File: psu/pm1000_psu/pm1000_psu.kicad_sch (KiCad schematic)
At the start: 42 parts, among them J1 , J2 , J3 , J4 , J5 , U1 LM317_TO-220, U2 LM317_TO-220, U3 LM317_TO-220

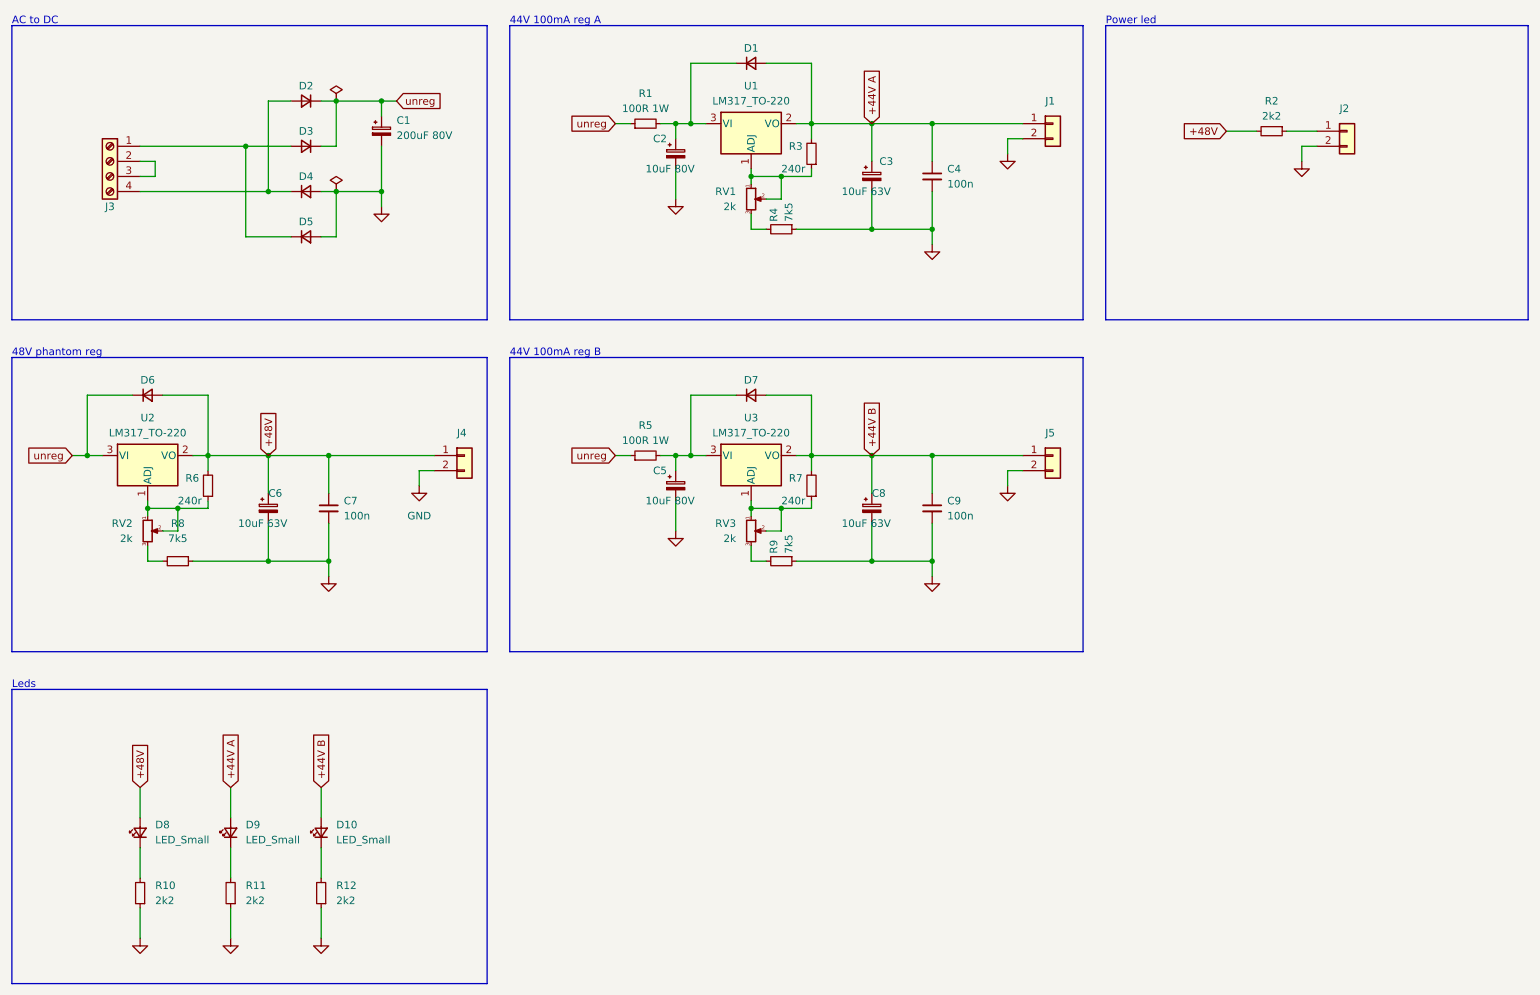
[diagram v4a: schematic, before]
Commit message: route psu pcb
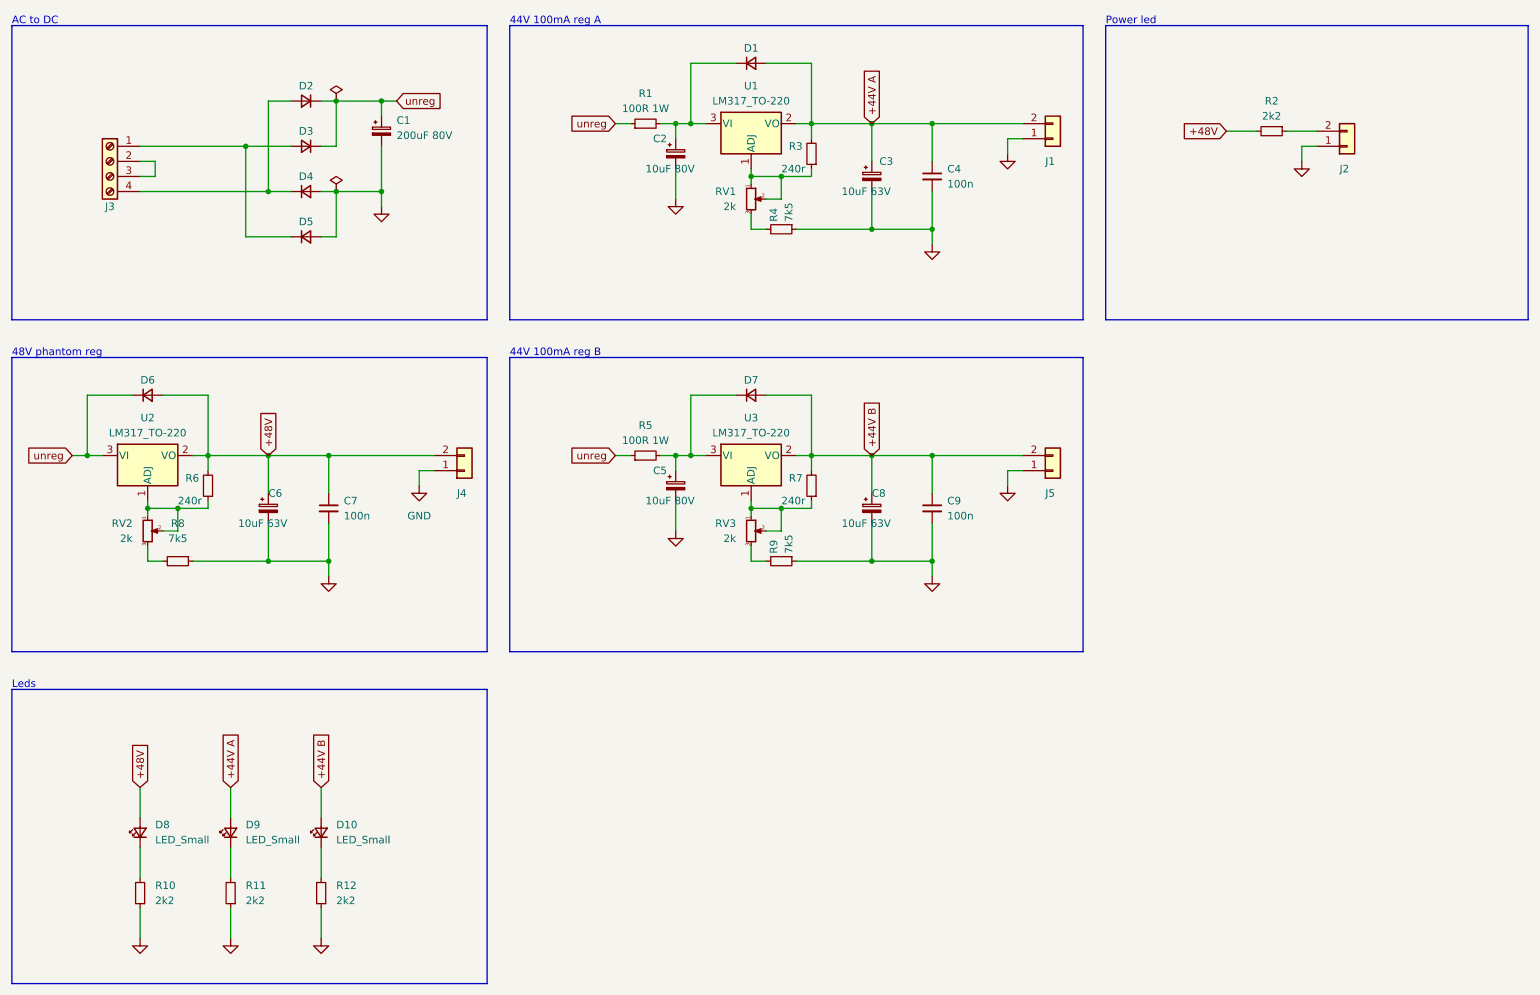
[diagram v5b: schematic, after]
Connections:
- net +44V A: now also J1.2 (Pin_2); no longer J1.1 (Pin_1)
- net +44V B: now also J5.2 (Pin_2); no longer J5.1 (Pin_1)
- net +48V: now also J4.2 (Pin_2); no longer J4.1 (Pin_1)
- net GND: now also J1.1 (Pin_1), J2.1 (Pin_1), J4.1 (Pin_1), J5.1 (Pin_1); no longer J1.2 (Pin_2), J2.2 (Pin_2), J4.2 (Pin_2), J5.2 (Pin_2)
- net at R2.1: now also J2.2 (Pin_2); no longer J2.1 (Pin_1)
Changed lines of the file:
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@@
     (pin "2")
   )
-  (symbol (lib_id "Connector_Generic:Conn_01x02") (at 196.85 93.98 0) (unit 1)
-    (in_bom yes) (on_board yes)
-    (property "Reference" "J5" (id 0) (at 195.58 90.17 0)
-      (effects (font (size 1.27 1.27)) (justify left))
-    )
-    (property "Value" " " (id 1) (at 194.31 100.33 0)
-      (effects (font (size 1.27 1.27)) (justify left))
-    )
-    (property "Footprint" "Connector_Molex:Molex_KK-396_5273-02A_1x02_P3.96mm_Vertical" (id 2) (at 196.85 93.98 0)
-      (effects (font (size 1.27 1.27)) hide)
-    )
-    (property "Datasheet" "~" (id 3) (at 196.85 93.98 0)
-      (effects (font (size 1.27 1.27)) hide)
-    )
-    (property "Function" "44V B" (id 4) (at 196.85 93.98 0)
-      (effects (font (size 1.27 1.27)) hide)
-    )
-    (pin "1")
-    (pin "2")
-  )
-  (symbol (lib_id "Connector_Generic:Conn_01x02") (at 97.79 93.98 0) (unit 1)
-    (in_bom yes) (on_board yes)
-    (property "Reference" "J4" (id 0) (at 96.52 90.17 0)
-      (effects (font (size 1.27 1.27)) (justify left))
-    )
-    (property "Value" " " (id 1) (at 91.44 99.06 0)
-      (effects (font (size 1.27 1.27)) (justify left))
-    )
-    (property "Footprint" "Connector_Molex:Molex_KK-254_AE-6410-02A_1x02_P2.54mm_Vertical" (id 2) (at 97.79 93.98 0)
-      (effects (font (size 1.27 1.27)) hide)
-    )
-    (property "Datasheet" "~" (id 3) (at 97.79 93.98 0)
-      (effects (font (size 1.27 1.27)) hide)
-    )
-    (property "Function" "48V phantom" (id 4) (at 97.79 93.98 0)
+  (symbol (lib_id "Connector_Generic:Conn_01x02") (at 196.85 96.52 0) (mirror x) (unit 1)
+    (in_bom yes) (on_board yes)
+    (property "Reference" "J5" (id 0) (at 195.58 100.33 0)
+      (effects (font (size 1.27 1.27)) (justify left))
+    )
+    (property "Value" " " (id 1) (at 194.31 90.17 0)
+      (effects (font (size 1.27 1.27)) (justify left))
+    )
+    (property "Footprint" "Connector_Molex:Molex_KK-396_5273-02A_1x02_P3.96mm_Vertical" (id 2) (at 196.85 96.52 0)
+      (effects (font (size 1.27 1.27)) hide)
+    )
+    (property "Datasheet" "~" (id 3) (at 196.85 96.52 0)
+      (effects (font (size 1.27 1.27)) hide)
+    )
+    (property "Function" "44V B" (id 4) (at 196.85 96.52 0)
+      (effects (font (size 1.27 1.27)) hide)
+    )
+    (pin "1")
+    (pin "2")
+  )
+  (symbol (lib_id "Connector_Generic:Conn_01x02") (at 97.79 96.52 0) (mirror x) (unit 1)
+    (in_bom yes) (on_board yes)
+    (property "Reference" "J4" (id 0) (at 96.52 100.33 0)
+      (effects (font (size 1.27 1.27)) (justify left))
+    )
+    (property "Value" " " (id 1) (at 91.44 91.44 0)
+      (effects (font (size 1.27 1.27)) (justify left))
+    )
+    (property "Footprint" "Connector_Molex:Molex_KK-254_AE-6410-02A_1x02_P2.54mm_Vertical" (id 2) (at 97.79 96.52 0)
+      (effects (font (size 1.27 1.27)) hide)
+    )
+    (property "Datasheet" "~" (id 3) (at 97.79 96.52 0)
+      (effects (font (size 1.27 1.27)) hide)
+    )
+    (property "Function" "48V phantom" (id 4) (at 97.79 96.52 0)
       (effects (font (size 1.27 1.27)) hide)
     )
@@
     (pin "1")
   )
-  (symbol (lib_id "Connector_Generic:Conn_01x02") (at 196.85 38.1 0) (unit 1)
-    (in_bom yes) (on_board yes)
-    (property "Reference" "J1" (id 0) (at 195.58 34.29 0)
-      (effects (font (size 1.27 1.27)) (justify left))
-    )
-    (property "Value" " " (id 1) (at 194.31 44.45 0)
-      (effects (font (size 1.27 1.27)) (justify left))
-    )
-    (property "Footprint" "Connector_Molex:Molex_KK-396_5273-02A_1x02_P3.96mm_Vertical" (id 2) (at 196.85 38.1 0)
-      (effects (font (size 1.27 1.27)) hide)
-    )
-    (property "Datasheet" "~" (id 3) (at 196.85 38.1 0)
-      (effects (font (size 1.27 1.27)) hide)
-    )
-    (property "Function" "44V A" (id 4) (at 196.85 38.1 0)
-      (effects (font (size 1.27 1.27)) hide)
-    )
-    (pin "1")
-    (pin "2")
-  )
-  (symbol (lib_id "Connector_Generic:Conn_01x02") (at 246.38 39.37 0) (unit 1)
-    (in_bom yes) (on_board yes)
-    (property "Reference" "J2" (id 0) (at 245.11 35.56 0)
-      (effects (font (size 1.27 1.27)) (justify left))
-    )
-    (property "Value" " " (id 1) (at 243.84 45.72 0)
-      (effects (font (size 1.27 1.27)) (justify left))
-    )
-    (property "Footprint" "Connector_Molex:Molex_KK-254_AE-6410-02A_1x02_P2.54mm_Vertical" (id 2) (at 246.38 39.37 0)
-      (effects (font (size 1.27 1.27)) hide)
-    )
-    (property "Datasheet" "~" (id 3) (at 246.38 39.37 0)
-      (effects (font (size 1.27 1.27)) hide)
-    )
-    (property "Function" "Power led" (id 4) (at 246.38 39.37 0)
-      (effects (font (size 1.27 1.27)) hide)
-    )
+  (symbol (lib_id "Connector_Generic:Conn_01x02") (at 196.85 40.64 0) (mirror x) (unit 1)
+    (in_bom yes) (on_board yes)
+    (property "Reference" "J1" (id 0) (at 195.58 44.45 0)
+      (effects (font (size 1.27 1.27)) (justify left))
+    )
+    (property "Value" " " (id 1) (at 194.31 34.29 0)
+      (effects (font (size 1.27 1.27)) (justify left))
+    )
+    (property "Footprint" "Connector_Molex:Molex_KK-396_5273-02A_1x02_P3.96mm_Vertical" (id 2) (at 196.85 40.64 0)
+      (effects (font (size 1.27 1.27)) hide)
+    )
+    (property "Datasheet" "~" (id 3) (at 196.85 40.64 0)
+      (effects (font (size 1.27 1.27)) hide)
+    )
+    (property "Function" "44V A" (id 4) (at 196.85 40.64 0)
+      (effects (font (size 1.27 1.27)) hide)
+    )
+    (pin "1")
+    (pin "2")
+  )
+  (symbol (lib_id "Connector_Generic:Conn_01x02") (at 246.38 41.91 0) (mirror x) (unit 1)
+    (in_bom yes) (on_board yes)
+    (property "Reference" "J2" (id 0) (at 245.11 45.72 0)
+      (effects (font (size 1.27 1.27)) (justify left))
+    )
+    (property "Value" " " (id 1) (at 243.84 35.56 0)
+      (effects (font (size 1.27 1.27)) (justify left))
+    )
+    (property "Footprint" "Connector_Molex:Molex_KK-254_AE-6410-02A_1x02_P2.54mm_Vertical" (id 2) (at 246.38 41.91 0)
+      (effects (font (size 1.27 1.27)) hide)
+    )
+    (property "Datasheet" "~" (id 3) (at 246.38 41.91 0)
+      (effects (font (size 1.27 1.27)) hide)
+    )
+    (property "Function" "Power led" (id 4) (at 246.38 41.91 0)
+      (effects (font (size 1.27 1.27)) hide)
+    )
